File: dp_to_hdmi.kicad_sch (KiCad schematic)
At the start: 1 part, among them U12 PS176

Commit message: Preliminary Revision of PS176 DP->HDMI Subsystem
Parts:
- added C100, C105, C108, C95, C97: 10uF, Capacitor_SMD:C_0402_1005Metric, symbol JLCImport:CL05A106MQ5NUNC
- added C101, C102, C103, C104, C27, C94: 1uF, Capacitor_SMD:C_0402_1005Metric, symbol JLCImport:CL05A105KA5NQNC
- added C106, C107, C96, C98, C99: 100nF, Capacitor_SMD:C_0402_1005Metric, symbol JLCImport:CL05B104KB54PNC
- added C89, C90: 18pF, Capacitor_SMD:C_0402_1005Metric, symbol JLCImport:0402CG180J500NT
- added C91: 4.7uF, Capacitor_SMD:C_0603_1608Metric, symbol JLCImport:CL10A475KO8NNNC
- added C92: 22uF, Capacitor_SMD:C_0603_1608Metric, symbol JLCImport:CL10A226MQ8NRNC
- added C93: 10pF, Capacitor_SMD:C_0603_1608Metric, symbol JLCImport:CL10C100JB8NNNC
- added L10: 1uH, TerminalBlock_Phoenix:TerminalBlock_Phoenix_PTSM-0,5-2-2,5-V-SMD_1x02-1MP_P2.50mm_Vertical, symbol JLCImport:FTC252012S1R0MBCA
- added L5, L6, L7, L8, L9: 330Ω@100MHz, JLCImport:BLM18KG331SN1D, symbol JLCImport:BLM18KG331SN1D
- added R53: 1k, Resistor_SMD:R_0402_1005Metric, symbol JLCImport:0402WGF1001TCE
- added R56, R69, R70: 10k, Resistor_SMD:R_0402_1005Metric, symbol JLCImport:0402WGF1002TCE
- added R57: 5.1k, Resistor_SMD:R_0402_1005Metric, symbol JLCImport:0402WGF5101TCE
- added R58, R65, R66, R71: 4.7k, Resistor_SMD:R_0402_1005Metric, symbol JLCImport:0402WGF4701TCE
- added R61, R62: 1k, Resistor_SMD:R_0402_1005Metric, symbol JLCImport:0402WGF5101TCE
- added R63, R64, R67, R68: 100k, Resistor_SMD:R_0402_1005Metric, symbol JLCImport:0402WGF1003TCE
- added U14: TLV62568DBVR, JLCImport:TLV62568DBVR, symbol JLCImport:TLV62568DBVR
- added X4: 27MHz 8pF 50Ω, JLCImport:5YMA27000121IF50E1, symbol JLCImport:5YMA27000121IF50E1
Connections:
- net DP_HPD: now also R53.1
- net PS176_VDD33: now reaches U12.1 (VDD33)
- net PS176_VDD33: now also U12.24 (VDD33), C95.2, C96.2, L8.1
- net at U12.10 (GPIO3): now also R58.2
- net PS_A12: now reaches U12.11 (VDDA12)
- net PS_A12: now also C108.2, L6.1
- net HDMI_CN: now reaches U12.13 (HDMICKN)
- net HDMI_CP: now reaches U12.14 (HDMICKP)
- net PS_TX12: now reaches U12.15 (VDDTX12)
- net PS_TX12: now also U12.18 (VDDTX12), C97.2, C98.2, C99.2, L9.1
- net HDMI_0N: now reaches U12.16 (HDMID0N)
- net HDMI_0P: now reaches U12.17 (HDMID0P)
- net HDMI_1N: now reaches U12.19 (HDMID1N)
- net HDMI_1P: now reaches U12.20 (HDMID1P)
- net HPDO: now reaches U12.21 (HDMI_HPD)
- net HDMI_2N: now reaches U12.22 (HDMID2N)
- net HDMI_2P: now reaches U12.23 (HDMID2P)
- net XTLO: now reaches U12.25 (XTLO)
- net XTLO: now also C89.2, X4.1
- net XTLI: now reaches U12.26 (XTLI)
- net XTLI: now also C90.2, X4.3
- net at U12.28 (CSDA): now also R66.1
- net at U12.29 (CSCL): now also R65.1
- net at U12.3 (I2C_ADDR): now also R71.2
- net PS176_VDD12: now reaches U12.30 (VDD12)
- net PS176_VDD12: now also U12.6 (VDD12), C100.2, L7.1
- net at U12.31 (AUXDCN): now also R64.1
- net at U12.32 (AUXDCP): now also R63.1
- net AUX-: now reaches U12.33 (AUXN)
- net AUX-: now also R61.1
- net AUX+: now reaches U12.34 (AUXP)
- net AUX+: now also R62.1
- net at U12.35 (RESETB): now also C27.2, R56.1
- net at U12.36 (REXT): now also R57.2
- net VDD12_ON: now reaches U12.37 (VDD12_ON)
- net VDD12_ON: now also R69.2, U14.1 (EN)
- net DP0+: now reaches U12.38 (DRX0P)
- net DP0-: now reaches U12.39 (DRX0N)
- net PS176_PWR_DN: now reaches U12.4 (PDB)
- net PS176_PWR_DN: now also R70.2
- net at U12.40 (DP_HPD): now also R53.2
- net DP1+: now reaches U12.41 (DRX1P)
- net DP1-: now reaches U12.42 (DRX1N)
- net PS_RX12: now reaches U12.43 (VDDRX12)
- net PS_RX12: now also U12.46 (VDDRX12), C105.2, C106.2, C107.2, L5.2
- net DP2+: now reaches U12.44 (DRX2P)
- net DP2-: now reaches U12.45 (DRX2N)
- net DP3+: now reaches U12.47 (DRX3P)
- net DP3-: now reaches U12.48 (DRX3N)
- net GND: now reaches U12.49 (EP)
- net GND: now also C100.1, C101.1, C102.1, C103.1, C104.1, C105.1, C106.1, C107.1, C108.1, C27.1, C89.1, C90.1, C91.1, C92.1, C93.1, C94.1, C95.1, C96.1, C97.1, C98.1, C99.1, R57.1, R58.1, R63.2, R68.1, U14.2 (GND), X4.2 (GND), X4.4 (GND)
- net HDMI_SCL: now reaches U12.7 (DDC_SCL)
- net HDMI_SDA: now reaches U12.8 (DDC_SDA)
- net CEC: now reaches U12.9 (HDMI_CEC)
- new net: R67.2, R68.2, U14.5 (FB)
- new net: L10.2, U14.3 (SW)
- new net +3V3: C91.2, C94.2, L8.2, R56.2, R61.2, R62.2, R64.2, R65.2, R66.2, R69.1, R70.1, R71.1, U14.4 (VIN)
- new net PS_VDD12: C101.2, C102.2, C103.2, C104.2, C92.2, C93.2, L10.1, L5.1, L6.2, L7.2, L9.2, R67.1
- no-connect marks 0 -> 4
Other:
- note added: "100nF AC coupling already added on TUSB1064 page"
- note added: "1k res for power sequencing protection"
- note added: "3V3->1V2 per WEBENCH"
- note added: "I2C_ADDR set to '1': 90h - 9Fh, D0h - DFh"
- note added: "May possibly connect PDB to MCU to save a tiny bit of power, if I feel so inclined."
- note added: "TODO: verify capacitance on crystal"
- title: (none) -> PS176 DP->HDMI Adapter Subsystem
- moved on the sheet: U12

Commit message: Preliminary design of USB2244i USB2.0 -> SD converter
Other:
- company: (none) -> Designed by: Matthew Kong
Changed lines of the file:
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@@
 		(title "PS176 DP->HDMI Adapter Subsystem")
 		(date "2026-05-02")
-		(rev "0.1")
+		(rev "1.0")
+		(company "Designed by: Matthew Kong")
 	)
 	(text "1k res for power\nsequencing protection"

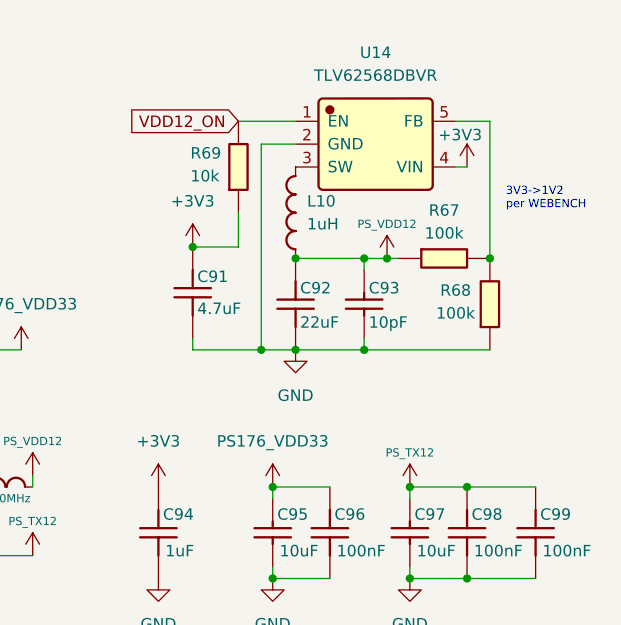
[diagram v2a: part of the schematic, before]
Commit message: Preliminary design of power monitor for PS176, TC358743, LicheeRV nano, and touch display
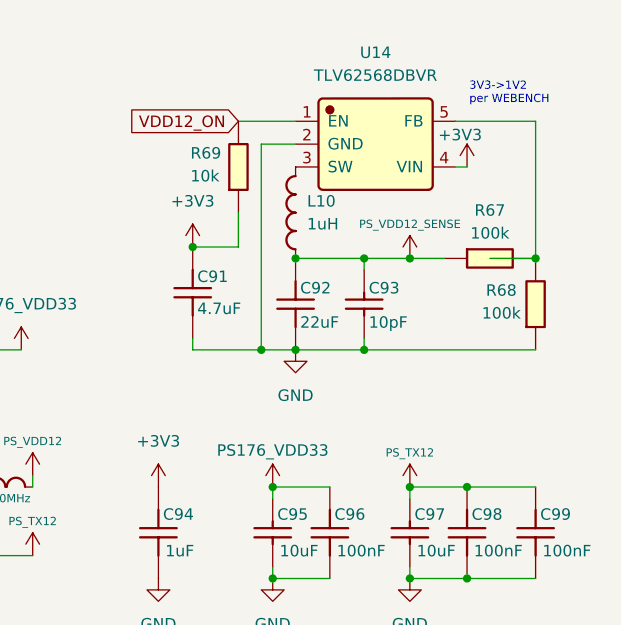
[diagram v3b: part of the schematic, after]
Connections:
- net PS_VDD12: no longer C92.2, C93.2, L10.1, R67.1
- new net PS_VDD12_SENSE: C92.2, C93.2, L10.1, R67.1
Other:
- moved on the sheet: R67, R68
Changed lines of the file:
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@@
 	(text "3V3->1V2\nper WEBENCH"
 		(exclude_from_sim no)
-		(at 185.928 32.766 0)
+		(at 181.864 21.082 0)
 		(effects
 			(font
@@
 	)
 	(junction
-		(at 184.15 39.37)
-		(diameter 0)
-		(color 0 0 0 0)
-	)
-	(junction
 		(at 53.34 43.18)
 		(diameter 0)
@@
 	)
 	(junction
-		(at 172.72 39.37)
-		(diameter 0)
-		(color 0 0 0 0)
-	)
-	(junction
 		(at 110.4901 57.15)
 		(diameter 0)
@@
 	)
 	(junction
-		(at 170.18 49.53)
-		(diameter 0)
-		(color 0 0 0 0)
-	)
-	(junction
 		(at 110.4901 54.61)
 		(diameter 0)
@@
 	)
 	(junction
+		(at 175.26 39.37)
+		(diameter 0)
+		(color 0 0 0 0)
+	)
+	(junction
 		(at 132.08 96.52)
 		(diameter 0)
@@
 	)
 	(junction
+		(at 189.23 39.37)
+		(diameter 0)
+		(color 0 0 0 0)
+	)
+	(junction
+		(at 170.18 49.53)
+		(diameter 0)
+		(color 0 0 0 0)
+	)
+	(junction
 		(at 58.42 116.84)
 		(diameter 0)
@@
 	(wire
 		(pts
-			(xy 170.18 49.53) (xy 184.15 49.53)
+			(xy 170.18 49.53) (xy 189.23 49.53)
 		)
 		(stroke
@@
 	(wire
 		(pts
+			(xy 189.23 39.37) (xy 184.15 39.37)
+		)
+		(stroke
+			(width 0)
+			(type default)
+		)
+	)
+	(wire
+		(pts
 			(xy 64.77 43.18) (xy 64.77 45.72)
 		)
@@
 	(wire
 		(pts
-			(xy 184.15 24.13) (xy 180.34 24.13)
+			(xy 189.23 24.13) (xy 180.34 24.13)
 		)
 		(stroke
@@
 	(wire
 		(pts
-			(xy 184.15 39.37) (xy 184.15 24.13)
+			(xy 189.23 39.37) (xy 189.23 24.13)
 		)
 		(stroke
@@
 	(wire
 		(pts
-			(xy 170.18 39.37) (xy 172.72 39.37)
+			(xy 170.18 39.37) (xy 175.26 39.37)
 		)
 		(stroke
@@
 	(wire
 		(pts
-			(xy 172.72 39.37) (xy 173.99 39.37)
+			(xy 158.75 49.53) (xy 162.56 49.53)
 		)
 		(stroke
@@
 	(wire
 		(pts
-			(xy 158.75 49.53) (xy 162.56 49.53)
+			(xy 58.42 116.84) (xy 58.42 114.3)
 		)
 		(stroke
@@
 	(wire
 		(pts
-			(xy 58.42 116.84) (xy 58.42 114.3)
+			(xy 175.26 39.37) (xy 179.07 39.37)
 		)
 		(stroke
@@
 		(in_pos_files yes)
 		(dnp no)
-		(fields_autoplaced yes)
 		(property "Reference" "#PWR0191"
 			(at 160.02 68.58 0)
@@
 		)
 		(property "Value" "PS176_VDD33"
-			(at 160.02 59.69 0)
+			(at 160.02 60.706 0)
 			(show_name no)
 			(do_not_autoplace no)
@@
 	(symbol
 		(lib_id "JLCImport:0402WGF1003TCE")
-		(at 184.15 44.45 90)
+		(at 189.23 44.45 90)
 		(unit 1)
 		(body_style 1)
@@
 		(dnp no)
 		(property "Reference" "R68"
-			(at 180.34 42.926 90)
+			(at 185.42 42.926 90)
 			(show_name no)
 			(do_not_autoplace no)
@@
 		)
 		(property "Value" "100k"
-			(at 180.34 45.466 90)
+			(at 185.42 45.466 90)
 			(show_name no)
 			(do_not_autoplace no)
@@
 		)
 		(property "Footprint" "Resistor_SMD:R_0402_1005Metric"
-			(at 184.15 44.45 0)
+			(at 189.23 44.45 0)
 			(hide yes)
 			(show_name no)
@@
 		)
 		(property "Datasheet" "https://www.lcsc.com/datasheet/lcsc_datasheet_2206010100_UNI-ROYAL-Uniroyal-Elec-0402WGF1003TCE_C25741.pdf"
-			(at 184.15 44.45 0)
+			(at 189.23 44.45 0)
 			(hide yes)
 			(show_name no)
@@
 		)
 		(property "Description" "-55℃~+155℃ 100kΩ 50V 62.5mW Thick Film Resistor ±1% ±100ppm/℃ 0402 Chip Resistor - Surface Mount ROHS"
-			(at 184.15 44.45 0)
+			(at 189.23 44.45 0)
 			(hide yes)
 			(show_name no)
@@
 		)
 		(property "LCSC" "C25741"
-			(at 184.15 44.45 0)
+			(at 189.23 44.45 0)
 			(hide yes)
 			(show_name no)
@@
 		)
 		(property "Manufacturer" "UNI-ROYAL(Uniroyal Elec)"
-			(at 184.15 44.45 0)
+			(at 189.23 44.45 0)
 			(hide yes)
 			(show_name no)
@@
 		)
 		(property "Manufacturer Part" "0402WGF1003TCE"
-			(at 184.15 44.45 0)
+			(at 189.23 44.45 0)
 			(hide yes)
 			(show_name no)
@@
 	(symbol
 		(lib_id "power:+3V3")
-		(at 172.72 39.37 0)
+		(at 175.26 39.37 0)
 		(unit 1)
 		(body_style 1)
@@
 		(dnp no)
 		(property "Reference" "#PWR0169"
-			(at 172.72 43.18 0)
+			(at 175.26 43.18 0)
 			(hide yes)
 			(show_name no)
@@
 			)
 		)
-		(property "Value" "PS_VDD12"
-			(at 172.72 35.56 0)
+		(property "Value" "PS_VDD12_SENSE"
+			(at 175.26 35.56 0)
 			(show_name no)
 			(do_not_autoplace no)
@@
 		)
 		(property "Footprint" ""
-			(at 172.72 39.37 0)
+			(at 175.26 39.37 0)
 			(hide yes)
 			(show_name no)
@@
 		)
 		(property "Datasheet" ""
-			(at 172.72 39.37 0)
+			(at 175.26 39.37 0)
 			(hide yes)
 			(show_name no)
@@
 		)
 		(property "Description" "Power symbol creates a global label with name \"+3V3\""
-			(at 172.72 39.37 0)
+			(at 175.26 39.37 0)
 			(hide yes)
 			(show_name no)
@@
 	(symbol
 		(lib_id "JLCImport:0402WGF1003TCE")
-		(at 179.07 39.37 0)
+		(at 184.15 39.37 0)
 		(unit 1)
 		(body_style 1)
@@
 		(dnp no)
 		(property "Reference" "R67"
-			(at 179.07 34.036 0)
+			(at 184.15 34.036 0)
 			(show_name no)
 			(do_not_autoplace no)
@@
 		)
 		(property "Value" "100k"
-			(at 179.07 36.576 0)
+			(at 184.15 36.576 0)
 			(show_name no)
 			(do_not_autoplace no)
@@
 		)
 		(property "Footprint" "Resistor_SMD:R_0402_1005Metric"
-			(at 179.07 39.37 0)
+			(at 184.15 39.37 0)
 			(hide yes)
 			(show_name no)
@@
 		)
 		(property "Datasheet" "https://www.lcsc.com/datasheet/lcsc_datasheet_2206010100_UNI-ROYAL-Uniroyal-Elec-0402WGF1003TCE_C25741.pdf"
-			(at 179.07 39.37 0)
+			(at 184.15 39.37 0)
 			(hide yes)
 			(show_name no)
@@
 		)
 		(property "Description" "-55℃~+155℃ 100kΩ 50V 62.5mW Thick Film Resistor ±1% ±100ppm/℃ 0402 Chip Resistor - Surface Mount ROHS"
-			(at 179.07 39.37 0)
+			(at 184.15 39.37 0)
 			(hide yes)
 			(show_name no)
@@
 		)
 		(property "LCSC" "C25741"
-			(at 179.07 39.37 0)
+			(at 184.15 39.37 0)
 			(hide yes)
 			(show_name no)
@@
 		)
 		(property "Manufacturer" "UNI-ROYAL(Uniroyal Elec)"
-			(at 179.07 39.37 0)
+			(at 184.15 39.37 0)
 			(hide yes)
 			(show_name no)
@@
 		)
 		(property "Manufacturer Part" "0402WGF1003TCE"
-			(at 179.07 39.37 0)
+			(at 184.15 39.37 0)
 			(hide yes)
 			(show_name no)
